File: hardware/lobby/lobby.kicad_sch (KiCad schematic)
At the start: 4 parts

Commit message: start routing mezzanine
making a progress capture before trying to cram a lot of signals onto just one hirose connector...
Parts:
- added J?: THD-02-R, Connector_PinHeader_2.54mm:PinHeader_2x02_P2.54mm_Vertical, symbol Connector_Generic:Conn_02x02_Odd_Even
- added J?: THD-20-R, Connector_PinHeader_2.54mm:PinHeader_2x20_P2.54mm_Vertical, symbol Connector_Generic:Conn_02x20_Odd_Even
- Module1: renamed from Module?; footprint CM4IO:Raspberry-Pi-4-Compute-Module -> cm4crypto:Raspberry-Pi-4-Compute-Module
- gave numbers to parts that had none: 2
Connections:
- net HDMI0_TX0_p is gone; now on net HDMI0_TX0_P: Module1.182 (HDMI0_TX0_P)
- net nPI_LED_Activity is gone; now on net nPI_LED_ACTIVITY: Module1.21 (PI_nLED_Activity)
- net +3.3v: now also J?.1 (Pin_1), J?.17 (Pin_17)
- net +5v: now also J?.2 (Pin_2), J?.4 (Pin_4)
- net GND: now also J?.14 (Pin_14), J?.20 (Pin_20), J?.25 (Pin_25), J?.30 (Pin_30), J?.34 (Pin_34), J?.39 (Pin_39), J?.6 (Pin_6), J?.9 (Pin_9)
- net GPIO2: now also J?.3 (Pin_3)
- net GPIO3: now also J?.5 (Pin_5)
- net GPIO4: now also J?.7 (Pin_7)
- net HDMI0_SDA: now also Module1.199 (HDMI0_SDA)
- net AnalogIP1: now reaches Module1.94 (AnalogIP1)
- net AnalogIP0: now reaches Module1.96 (AnalogIP0)
- new net GPIO10: J?.19 (Pin_19)
- new net GPIO11: J?.23 (Pin_23)
- new net GPIO12: J?.32 (Pin_32)
- new net GPIO13: J?.33 (Pin_33)
- new net GPIO14: J?.8 (Pin_8)
- new net GPIO15: J?.10 (Pin_10)
- new net GPIO16: J?.36 (Pin_36)
- new net GPIO17: J?.11 (Pin_11)
- new net GPIO18: J?.12 (Pin_12)
- new net GPIO19: J?.35 (Pin_35)
- new net GPIO20: J?.38 (Pin_38)
- new net GPIO21: J?.40 (Pin_40)
- new net GPIO22: J?.15 (Pin_15)
- new net GPIO23: J?.16 (Pin_16)
- new net GPIO24: J?.18 (Pin_18)
- new net GPIO25: J?.22 (Pin_22)
- new net GPIO26: J?.37 (Pin_37)
- new net GPIO27: J?.13 (Pin_13)
- new net GPIO5: J?.29 (Pin_29)
- new net GPIO6: J?.31 (Pin_31)
- new net GPIO7: J?.26 (Pin_26)
- new net GPIO8: J?.24 (Pin_24)
- new net GPIO9: J?.21 (Pin_21)
- new net ID_SC: J?.28 (Pin_28)
- new net ID_SD: J?.27 (Pin_27)
- new net TR0_TAP: J?.3 (Pin_3)
- new net TR1_TAP: J?.1 (Pin_1)
- new net TR2_TAP: J?.2 (Pin_2)
- new net TR3_TAP: J?.4 (Pin_4)
- no-connect marks 34 -> 66
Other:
- sheet escalator ports: added AnalogIP0, AnalogIP1, nPI_LED_ACTIVITY; removed nPI_LED_Activity
- note added: "40Way GPIO Header"

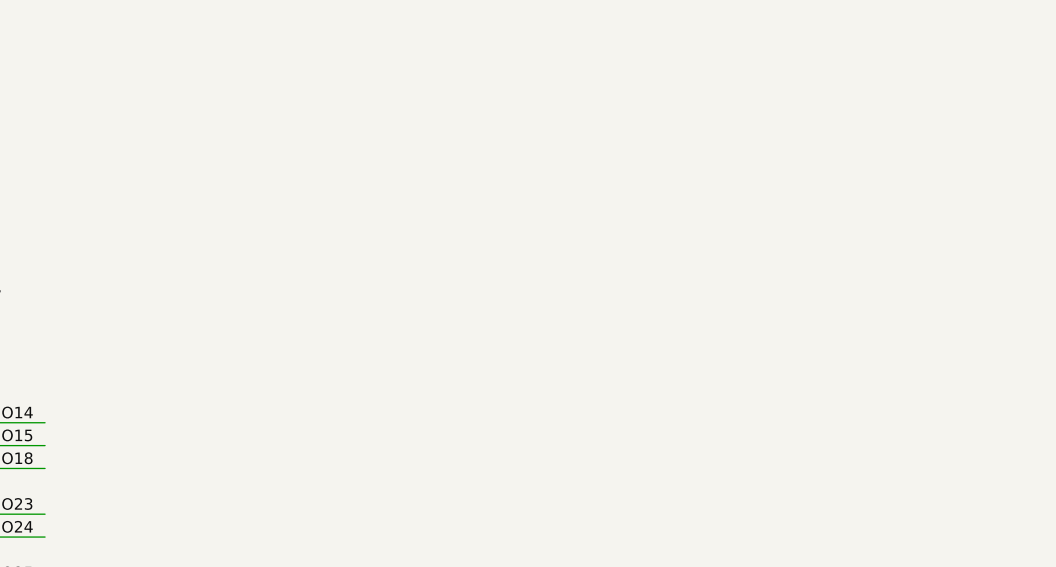
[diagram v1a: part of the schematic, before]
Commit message: finished mezzanine signal routing
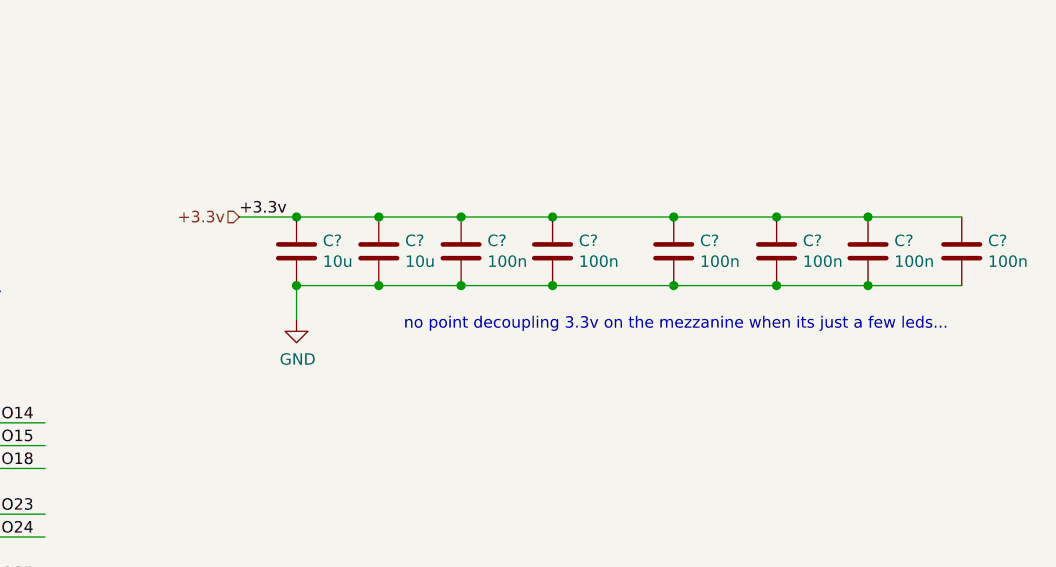
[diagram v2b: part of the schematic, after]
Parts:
- added C? (x6): 100n, Capacitor_SMD:C_0402_1005Metric, symbol Device:C
- added C? (x2): 10u, Capacitor_SMD:C_0805_2012Metric, symbol Device:C
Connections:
- net +3.3v: now also C?.1, C?.1, C?.1, C?.1, C?.1, C?.1, C?.1, C?.1
- net GND: now also C?.2, C?.2, C?.2, C?.2, C?.2, C?.2, C?.2, C?.2
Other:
- note added: "no point decoupling 3.3v on the mezzanine when its just a few leds..."

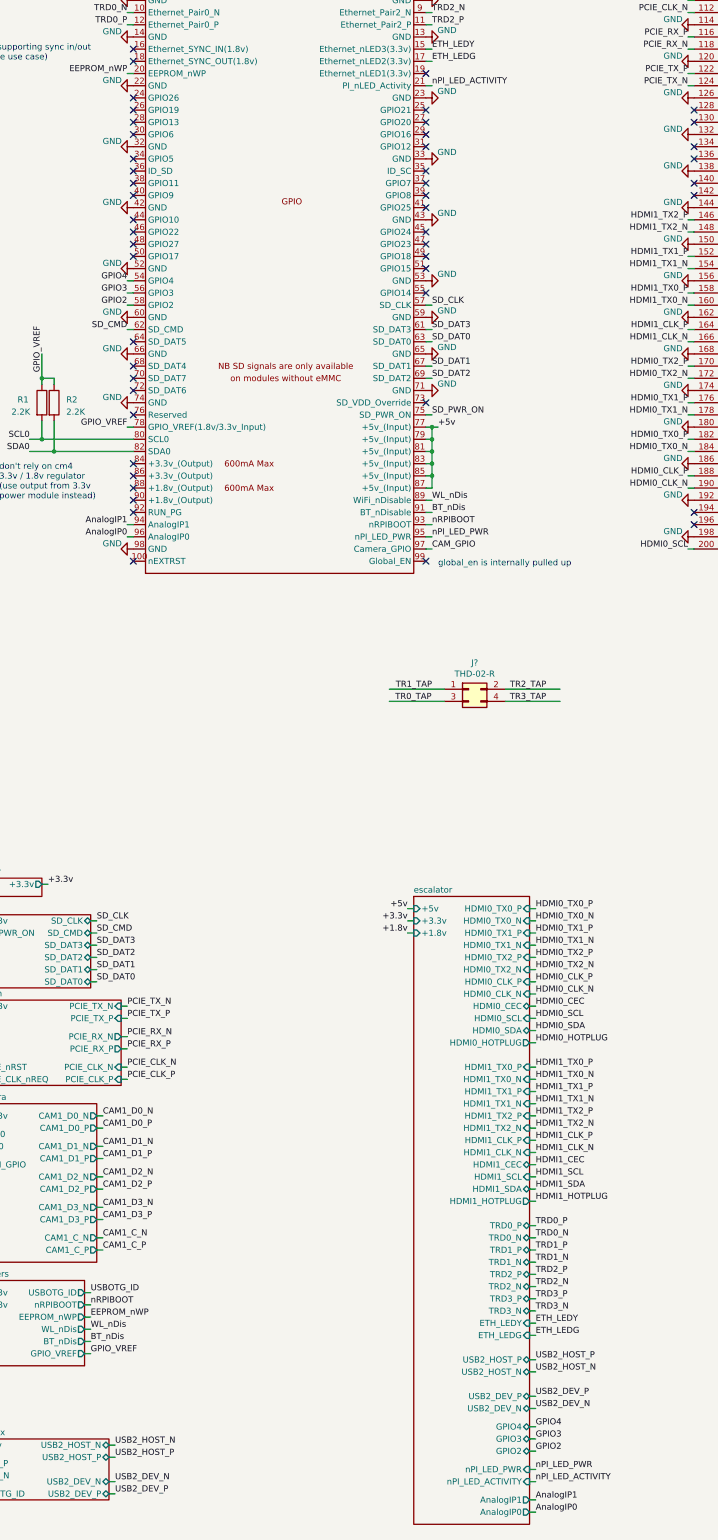
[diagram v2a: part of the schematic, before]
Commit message: sheet refs relative, copied escalator pinout to lobby
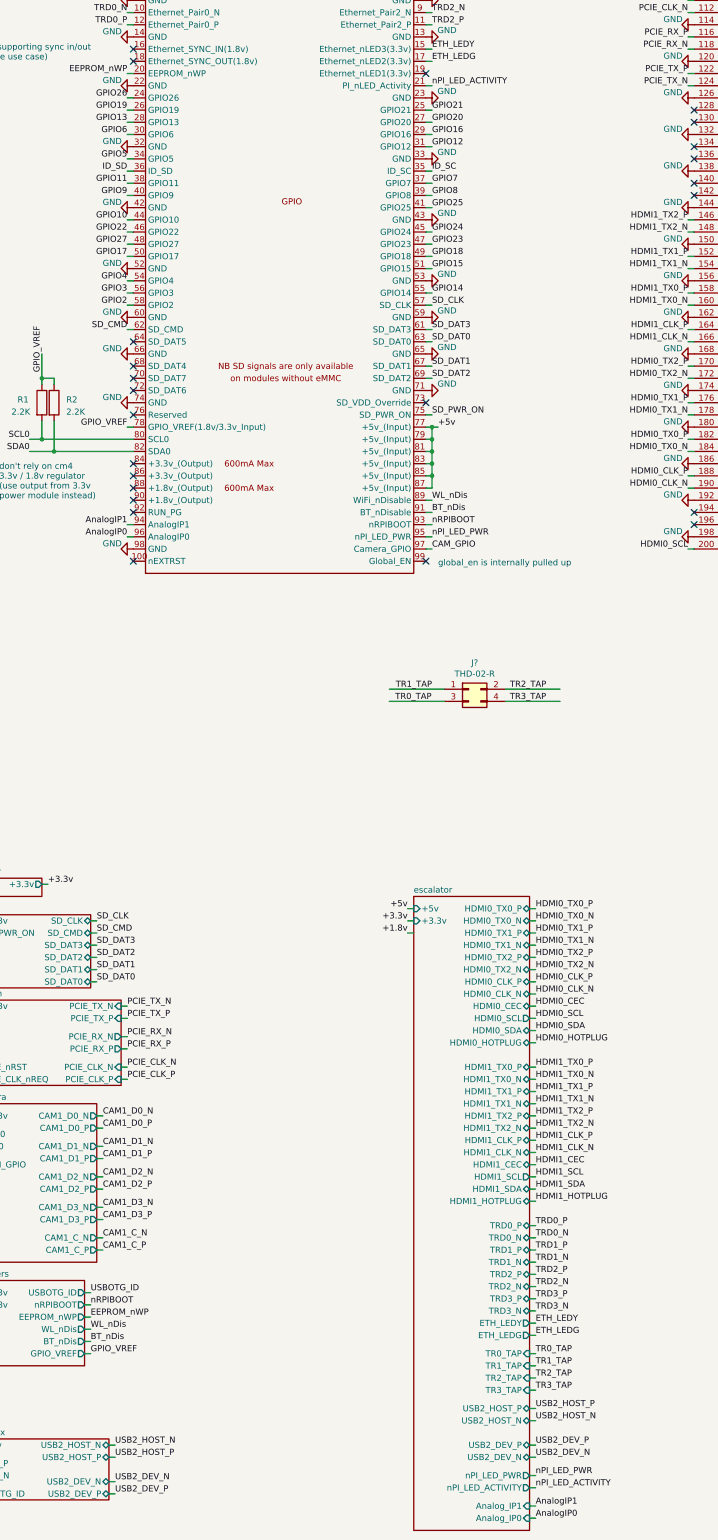
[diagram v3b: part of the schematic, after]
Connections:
- net GPIO10: now also Module1.44 (GPIO10)
- net GPIO11: now also Module1.38 (GPIO11)
- net GPIO12: now also Module1.31 (GPIO12)
- net GPIO13: now also Module1.28 (GPIO13)
- net GPIO14: now also Module1.55 (GPIO14)
- net GPIO15: now also Module1.51 (GPIO15)
- net GPIO16: now also Module1.29 (GPIO16)
- net GPIO17: now also Module1.50 (GPIO17)
- net GPIO18: now also Module1.49 (GPIO18)
- net GPIO19: now also Module1.26 (GPIO19)
- net GPIO20: now also Module1.27 (GPIO20)
- net GPIO21: now also Module1.25 (GPIO21)
- net GPIO22: now also Module1.46 (GPIO22)
- net GPIO23: now also Module1.47 (GPIO23)
- net GPIO24: now also Module1.45 (GPIO24)
- net GPIO25: now also Module1.41 (GPIO25)
- net GPIO26: now also Module1.24 (GPIO26)
- net GPIO27: now also Module1.48 (GPIO27)
- net GPIO5: now also Module1.34 (GPIO5)
- net GPIO6: now also Module1.30 (GPIO6)
- net GPIO7: now also Module1.37 (GPIO7)
- net GPIO8: now also Module1.39 (GPIO8)
- net GPIO9: now also Module1.40 (GPIO9)
- net ID_SC: now also Module1.35 (ID_SC)
- net ID_SD: now also Module1.36 (ID_SD)
- no-connect marks 66 -> 41
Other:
- sheet camera: file C:\Users\Lyocek\Desktop\Tmp\cm4crypto\hardware\lobby\sheets\camera.kicad_sch -> ./sheets/camera.kicad_sch
- sheet escalator: file C:\Users\Lyocek\Desktop\Tmp\cm4crypto\hardware\lobby\sheets\escalator.kicad_sch -> ./sheets/escalator.kicad_sch
- sheet escalator ports: added Analog_IP0, Analog_IP1, TR0_TAP, TR1_TAP, TR2_TAP, TR3_TAP; removed +1.8v, AnalogIP0, AnalogIP1, GPIO2, GPIO3, GPIO4
- sheet jumpers: file C:\Users\Lyocek\Desktop\Tmp\cm4crypto\hardware\lobby\sheets\jumpers.kicad_sch -> ./sheets/jumpers.kicad_sch
- sheet m.2-m: file C:\Users\Lyocek\Desktop\Tmp\cm4crypto\hardware\lobby\sheets\m.2-m.kicad_sch -> ./sheets/m.2-m.kicad_sch
- sheet power: file C:\Users\Lyocek\Desktop\Tmp\cm4crypto\hardware\lobby\sheets\power.kicad_sch -> ./sheets/power.kicad_sch
- sheet sd: file C:\Users\Lyocek\Desktop\Tmp\cm4crypto\hardware\lobby\sheets\sd.kicad_sch -> ./sheets/sd.kicad_sch
- sheet usb-mux: file C:\Users\Lyocek\Desktop\Tmp\cm4crypto\hardware\lobby\sheets\usb-mux.kicad_sch -> ./sheets/usb-mux.kicad_sch

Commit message: work abroad
did some light planning for the lobby board while on vacation. now ready for final placement + routing
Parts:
- removed C? (x6): 100n, Capacitor_SMD:C_0402_1005Metric, symbol Device:C
- removed C? (x2): 10u, Capacitor_SMD:C_0805_2012Metric, symbol Device:C
- gave numbers to parts that had none: 2
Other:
- note removed: "no point decoupling 3.3v on the mezzanine when its just a few leds..."

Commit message: removed gpio from lobby to simplify routing
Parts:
- J2: footprint Connector_PinHeader_2.54mm:PinHeader_2x20_P2.54mm_Vertical -> cm4crypto:rpi-40-just-power; symbol Connector_Generic:Conn_02x20_Odd_Even -> cm4crypto:rpi-40-jus-power
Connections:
- net +3.3v: no longer J2.17 (Pin_17)
- net GND: no longer J2.14 (Pin_14), J2.20 (Pin_20), J2.25 (Pin_25), J2.30 (Pin_30), J2.34 (Pin_34), J2.39 (Pin_39), J2.9 (Pin_9)
- net GPIO10: no longer J2.19 (Pin_19)
- net GPIO11: no longer J2.23 (Pin_23)
- net GPIO12: no longer J2.32 (Pin_32)
- net GPIO13: no longer J2.33 (Pin_33)
- net GPIO15: no longer J2.10 (Pin_10)
- net GPIO16: no longer J2.36 (Pin_36)
- net GPIO17: no longer J2.11 (Pin_11)
- net GPIO18: no longer J2.12 (Pin_12)
- net GPIO19: no longer J2.35 (Pin_35)
- net GPIO20: no longer J2.38 (Pin_38)
- net GPIO21: no longer J2.40 (Pin_40)
- net GPIO22: no longer J2.15 (Pin_15)
- net GPIO23: no longer J2.16 (Pin_16)
- net GPIO24: no longer J2.18 (Pin_18)
- net GPIO25: no longer J2.22 (Pin_22)
- net GPIO26: no longer J2.37 (Pin_37)
- net GPIO27: no longer J2.13 (Pin_13)
- net GPIO4: no longer J2.7 (Pin_7)
- net GPIO5: no longer J2.29 (Pin_29)
- net GPIO6: no longer J2.31 (Pin_31)
- net GPIO7: no longer J2.26 (Pin_26)
- net GPIO8: no longer J2.24 (Pin_24)
- net GPIO9: no longer J2.21 (Pin_21)
- net ID_SC: no longer J2.28 (Pin_28)
- net ID_SD: no longer J2.27 (Pin_27)

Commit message: finish routing on lobby
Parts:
- added R8, R9: 2.2K, Resistor_SMD:R_0603_1608Metric, symbol Device:R
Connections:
- net +1.8v: now also Module1.88 (+1.8v_(Output)), Module1.90 (+1.8v_(Output))
- net GPIO2: now also R8.2
- net GPIO3: now also R9.2
- net GPIO_VREF: now also R8.1, R9.1
- no-connect marks 41 -> 39
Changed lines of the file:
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@@
   (junction (at 26.67 125.73) (diameter 0.9144) (color 0 0 0 0))
   (junction (at 29.21 128.27) (diameter 0.9144) (color 0 0 0 0))
+  (junction (at 44.45 135.89) (diameter 0.9144) (color 0 0 0 0))
   (junction (at 107.95 123.19) (diameter 0.9144) (color 0 0 0 0))
   (junction (at 107.95 125.73) (diameter 0.9144) (color 0 0 0 0))
@@
   (junction (at 107.95 130.81) (diameter 0.9144) (color 0 0 0 0))
   (junction (at 107.95 133.35) (diameter 0.9144) (color 0 0 0 0))
+  (junction (at 184.15 234.95) (diameter 0.9144) (color 0 0 0 0))
+  (junction (at 186.69 237.49) (diameter 0.9144) (color 0 0 0 0))
+  (junction (at 186.69 250.19) (diameter 0.9144) (color 0 0 0 0))
   (junction (at 201.93 232.41) (diameter 1.016) (color 0 0 0 0))
   (no_connect (at 45.72 44.45))
@@
   (no_connect (at 45.72 130.81))
   (no_connect (at 45.72 133.35))
-  (no_connect (at 45.72 135.89))
-  (no_connect (at 45.72 138.43))
   (no_connect (at 45.72 140.97))
   (no_connect (at 45.72 151.13))
@@
     (stroke (width 0) (type solid) (color 0 0 0 0))
   )
+  (wire (pts (xy 43.18 135.89) (xy 44.45 135.89))
+    (stroke (width 0) (type solid) (color 0 0 0 0))
+  )
   (wire (pts (xy 43.18 243.84) (xy 44.45 243.84))
     (stroke (width 0) (type solid) (color 0 0 0 0))
@@
     (stroke (width 0) (type solid) (color 0 0 0 0))
   )
+  (wire (pts (xy 44.45 135.89) (xy 44.45 138.43))
+    (stroke (width 0) (type solid) (color 0 0 0 0))
+  )
+  (wire (pts (xy 44.45 135.89) (xy 45.72 135.89))
+    (stroke (width 0) (type solid) (color 0 0 0 0))
+  )
   (wire (pts (xy 44.45 143.51) (xy 45.72 143.51))
     (stroke (width 0) (type solid) (color 0 0 0 0))
@@
     (stroke (width 0) (type solid) (color 0 0 0 0))
   )
+  (wire (pts (xy 45.72 138.43) (xy 44.45 138.43))
+    (stroke (width 0) (type solid) (color 0 0 0 0))
+  )
   (wire (pts (xy 99.06 177.8) (xy 110.49 177.8))
     (stroke (width 0) (type solid) (color 0 0 0 0))
@@
     (stroke (width 0) (type solid) (color 0 0 0 0))
   )
-  (wire (pts (xy 176.53 234.95) (xy 187.96 234.95))
+  (wire (pts (xy 176.53 234.95) (xy 184.15 234.95))
     (stroke (width 0) (type solid) (color 0 0 0 0))
   )
-  (wire (pts (xy 176.53 237.49) (xy 187.96 237.49))
+  (wire (pts (xy 176.53 237.49) (xy 186.69 237.49))
     (stroke (width 0) (type solid) (color 0 0 0 0))
   )
@@
     (stroke (width 0) (type solid) (color 0 0 0 0))
   )
+  (wire (pts (xy 184.15 234.95) (xy 187.96 234.95))
+    (stroke (width 0) (type solid) (color 0 0 0 0))
+  )
+  (wire (pts (xy 184.15 241.3) (xy 184.15 234.95))
+    (stroke (width 0) (type solid) (color 0 0 0 0))
+  )
+  (wire (pts (xy 184.15 248.92) (xy 184.15 250.19))
+    (stroke (width 0) (type solid) (color 0 0 0 0))
+  )
+  (wire (pts (xy 186.69 237.49) (xy 187.96 237.49))
+    (stroke (width 0) (type solid) (color 0 0 0 0))
+  )
+  (wire (pts (xy 186.69 241.3) (xy 186.69 237.49))
+    (stroke (width 0) (type solid) (color 0 0 0 0))
+  )
+  (wire (pts (xy 186.69 250.19) (xy 184.15 250.19))
+    (stroke (width 0) (type solid) (color 0 0 0 0))
+  )
+  (wire (pts (xy 186.69 250.19) (xy 186.69 248.92))
+    (stroke (width 0) (type solid) (color 0 0 0 0))
+  )
+  (wire (pts (xy 186.69 255.27) (xy 186.69 250.19))
+    (stroke (width 0) (type solid) (color 0 0 0 0))
+  )
   (wire (pts (xy 200.66 232.41) (xy 201.93 232.41))
     (stroke (width 0) (type solid) (color 0 0 0 0))
@@
     (effects (font (size 1.27 1.27)) (justify left bottom))
   )
+  (label "+1.8v" (at 43.18 135.89 180)
+    (effects (font (size 1.27 1.27)) (justify right bottom))
+  )
   (label "TRD1_P" (at 44.45 29.21 180)
     (effects (font (size 1.27 1.27)) (justify right bottom))
@@
     (effects (font (size 1.27 1.27)) (justify right bottom))
   )
+  (label "GPIO_VREF" (at 186.69 251.46 270)
+    (effects (font (size 1.27 1.27)) (justify right bottom))
+  )
   (label "+5v" (at 205.74 232.41 180)
     (effects (font (size 1.27 1.27)) (justify right bottom))
@@
     (pin "2")
   )
+  (symbol (lib_id "Device:R") (at 184.15 245.11 180) (unit 1)
+    (in_bom yes) (on_board yes)
+    (property "Reference" "R8" (id 0) (at 181.61 245.7451 0)
+      (effects (font (size 1.27 1.27)) (justify left))
+    )
+    (property "Value" "2.2K" (id 1) (at 181.61 243.2051 0)
+      (effects (font (size 1.27 1.27)) (justify left))
+    )
+    (property "Footprint" "Resistor_SMD:R_0603_1608Metric" (id 2) (at 185.928 245.11 90)
+      (effects (font (size 1.27 1.27)) hide)
+    )
+    (property "Datasheet" "~" (id 3) (at 184.15 245.11 0)
+      (effects (font (size 1.27 1.27)) hide)
+    )
+    (pin "1")
+    (pin "2")
+  )
+  (symbol (lib_id "Device:R") (at 186.69 245.11 180) (unit 1)
+    (in_bom yes) (on_board yes)
+    (property "Reference" "R9" (id 0) (at 191.77 245.7451 0)
+      (effects (font (size 1.27 1.27)) (justify left))
+    )
+    (property "Value" "2.2K" (id 1) (at 193.04 243.2051 0)
+      (effects (font (size 1.27 1.27)) (justify left))
+    )
+    (property "Footprint" "Resistor_SMD:R_0603_1608Metric" (id 2) (at 188.468 245.11 90)
+      (effects (font (size 1.27 1.27)) hide)
+    )
+    (property "Datasheet" "~" (id 3) (at 186.69 245.11 0)
+      (effects (font (size 1.27 1.27)) hide)
+    )
+    (pin "1")
+    (pin "2")
+  )
   (symbol (lib_id "Connector_Generic:Conn_02x02_Odd_Even") (at 115.57 177.8 0) (unit 1)
     (in_bom yes) (on_board yes)
@@
       (reference "R2") (unit 1) (value "2.2K") (footprint "Resistor_SMD:R_0603_1608Metric")
     )
+    (path "/ee42ed9d-4f49-4ce9-8516-7fb1e6cbe849"
+      (reference "R8") (unit 1) (value "2.2K") (footprint "Resistor_SMD:R_0603_1608Metric")
+    )
+    (path "/ceb5b92e-0ae0-4b56-9c5f-259b67e98e24"
+      (reference "R9") (unit 1) (value "2.2K") (footprint "Resistor_SMD:R_0603_1608Metric")
+    )
     (path "/6e4a2eb6-41a2-4d83-9a3f-0b4c7a46017c/fff0a41f-5964-4739-8a09-f6b09dc512ba"

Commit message: tweak lobby
pushed traces for wifi clearance zone
improved cm4 footprint
improved usb-c footprint
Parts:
- Module1: footprint cm4crypto:Raspberry-Pi-4-Compute-Module -> cm4crypto:Raspberry-Pi-4-Compute-Module-diagonal-mount-bl-ur
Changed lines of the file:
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@@
     (property "Reference" "Module1" (id 0) (at 193.04 12.7 0))
     (property "Value" "ComputeModule4-CM4" (id 1) (at 193.04 15.24 0))
-    (property "Footprint" "cm4crypto:Raspberry-Pi-4-Compute-Module" (id 2) (at 195.58 111.76 0)
+    (property "Footprint" "cm4crypto:Raspberry-Pi-4-Compute-Module-diagonal-mount-bl-ur" (id 2) (at 195.58 111.76 0)
       (effects (font (size 1.27 1.27)) hide)
     )
@@
     (property "Reference" "Module1" (id 0) (at 76.2 15.24 0))
     (property "Value" "ComputeModule4-CM4" (id 1) (at 76.2 17.78 0))
-    (property "Footprint" "cm4crypto:Raspberry-Pi-4-Compute-Module" (id 2) (at 220.98 109.22 0)
+    (property "Footprint" "cm4crypto:Raspberry-Pi-4-Compute-Module-diagonal-mount-bl-ur" (id 2) (at 220.98 109.22 0)
       (effects (font (size 1.27 1.27)) hide)
     )
@@
     )
     (path "/9f8c7c9e-f209-4a15-a904-9871f0b04ae7"
-      (reference "Module1") (unit 1) (value "ComputeModule4-CM4") (footprint "cm4crypto:Raspberry-Pi-4-Compute-Module")
+      (reference "Module1") (unit 1) (value "ComputeModule4-CM4") (footprint "cm4crypto:Raspberry-Pi-4-Compute-Module-diagonal-mount-bl-ur")
     )
     (path "/ae2ff523-15be-4cb4-ab50-2c31b9f52a22"
-      (reference "Module1") (unit 2) (value "ComputeModule4-CM4") (footprint "cm4crypto:Raspberry-Pi-4-Compute-Module")
+      (reference "Module1") (unit 2) (value "ComputeModule4-CM4") (footprint "cm4crypto:Raspberry-Pi-4-Compute-Module-diagonal-mount-bl-ur")
     )
     (path "/c1ce5a38-066f-4e37-8f93-41dc0889376a"
